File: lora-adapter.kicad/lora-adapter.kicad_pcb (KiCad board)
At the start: 2 copper layers, 36 x 31.9 mm, 6 parts, among them J1 Conn_LoRa, U1 RFM9x_Lora_Breakout

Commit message: LoRa-adapter: Rev 1.00 ready for production
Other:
- board text added: "https://github.com/ bablokb/pcb-pico-datalogger LoRa-Adapter Rev. 1.00"
- board text removed: "https://github.com/ bablokb/pcb-pico-datalogger LoRa-Adapter Rev. 0.90"

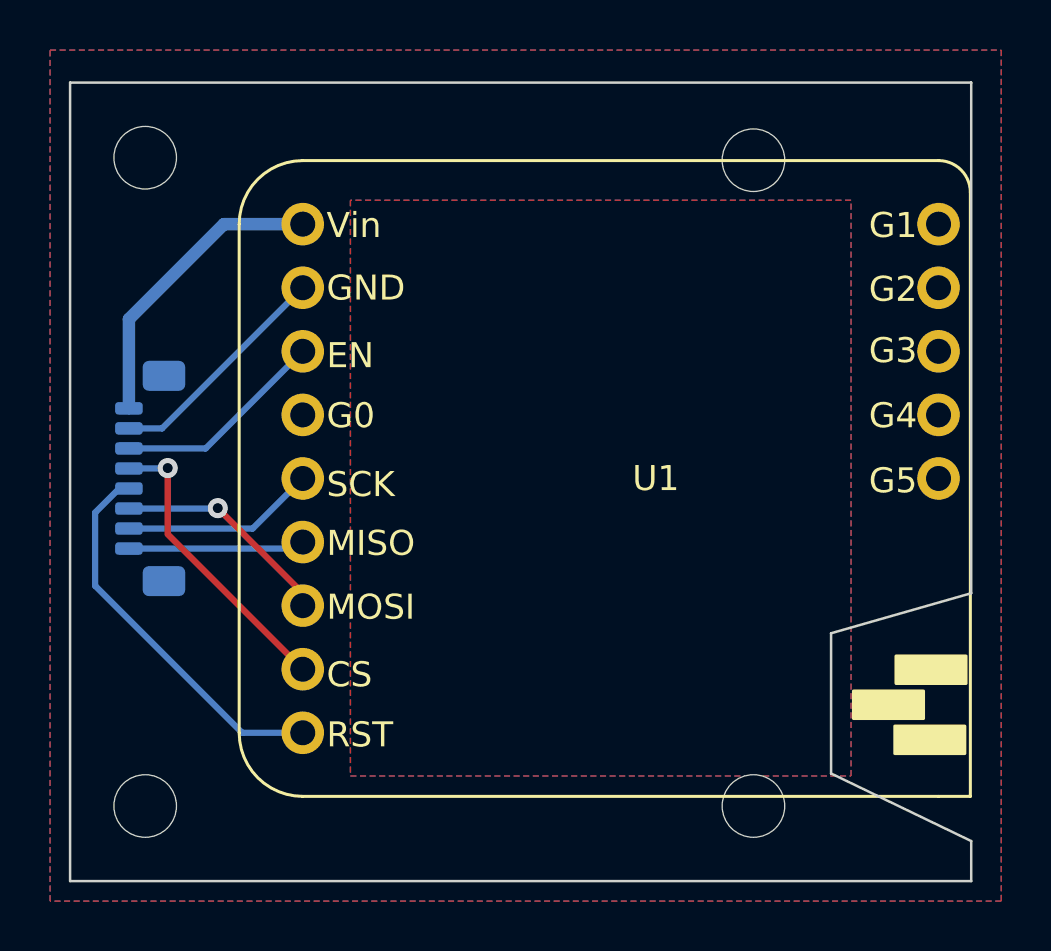
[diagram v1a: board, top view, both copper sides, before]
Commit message: LoRa-Adaper Rev 1.10: add pin-sockets to board (and production files)
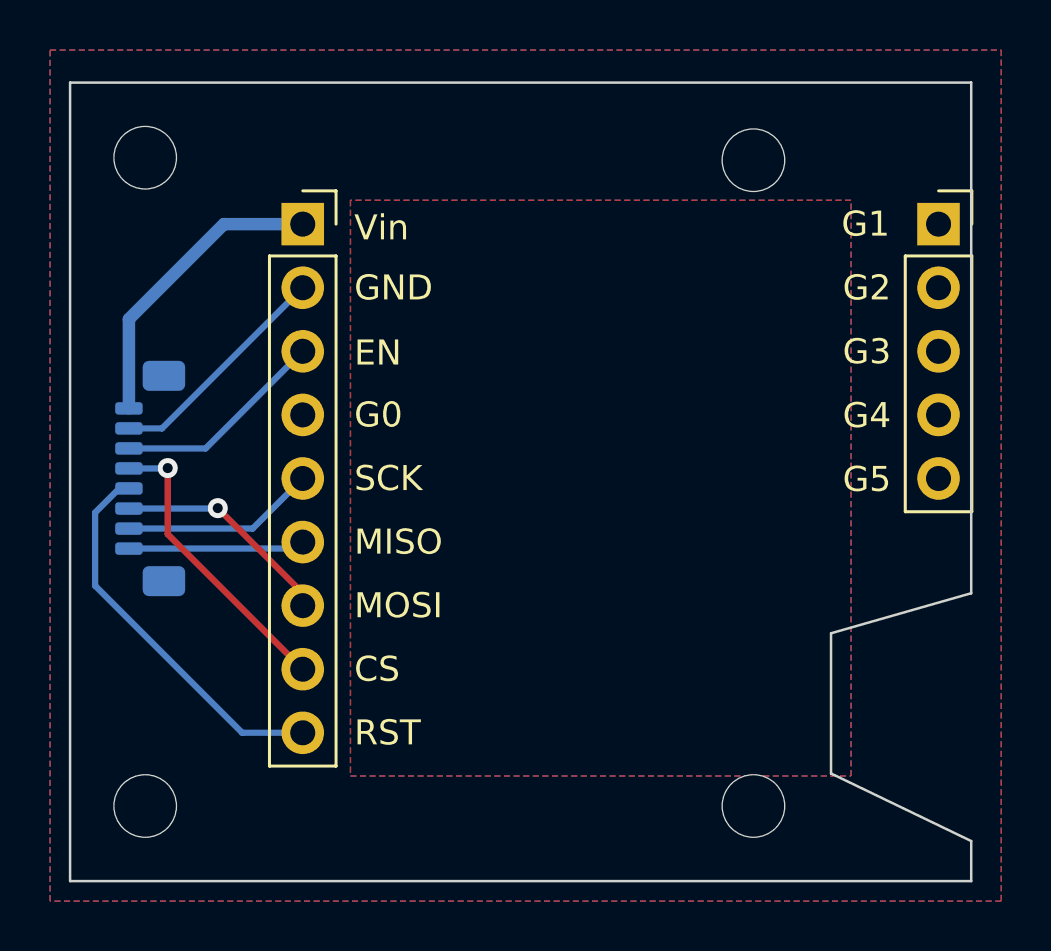
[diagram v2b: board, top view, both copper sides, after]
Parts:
- added J2: Conn_01x05, Connector_PinSocket_2.54mm:PinSocket_1x05_P2.54mm_Vertical, F.Cu at (170.5, 78.0)
- U1: footprint user:RFM9x_Lora_Breakout -> Connector_PinSocket_2.54mm:PinSocket_1x09_P2.54mm_Vertical
- turned U1 to 0 degrees
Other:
- board text added: "3V3"
- board text added: "CS"
- board text added: "EN"
- board text added: "G0"
- board text added: "G1"
- board text added: "G2"
- board text added: "G3"
- board text added: "G4"
- board text added: "G5"
- board text added: "GND"
- board text added: "MISO"
- board text added: "MISO1"
- board text added: "MOSI"
- board text added: "RST"
- board text added: "SCK"
- board text added: "Vin"
- board text added: "https://github.com/ bablokb/pcb-pico-datalogger LoRa-Adapter Rev. 1.10"
- board text removed: "https://github.com/ bablokb/pcb-pico-datalogger LoRa-Adapter Rev. 1.00"

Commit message: LoRa-Adaper Rev 1.20: move SUR-connector to top
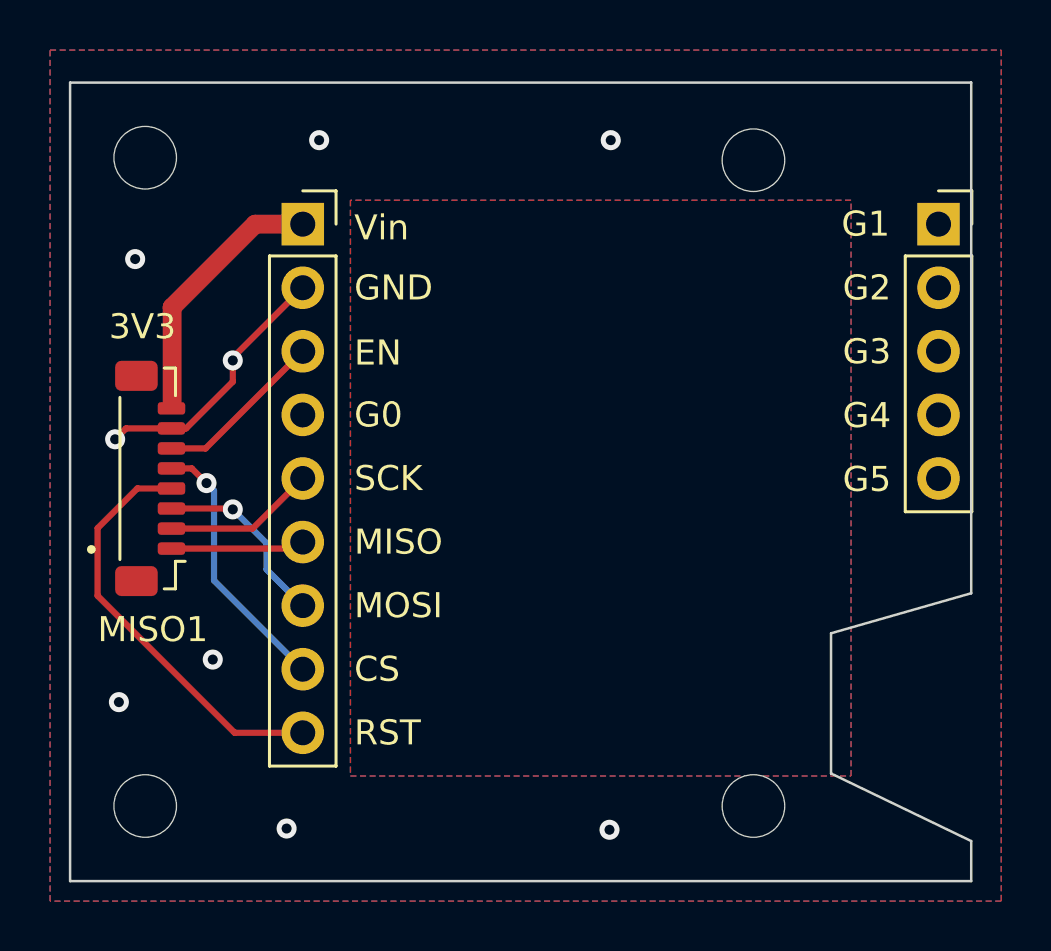
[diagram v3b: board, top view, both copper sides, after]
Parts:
- J1: moved to F.Cu
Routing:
- net /SCLK1: track 7.77 -> 6.07 mm
- net /MISO1: track 7.05 -> 5.35 mm
- net /Lora_EN: track 8.55 -> 6.85 mm
- net +3V3: track 12.1 -> 10.5 mm
- net /MOSI1: track 8.86 -> 7.47 mm
- net /Lora_RST: track 15.4 -> 16.8 mm
- net GND: track 9.27 -> 10.6 mm, vias 0 -> 9
- net /Lora_CS: track 11.8 -> 10.7 mm
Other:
- board text added: "https://github.com/ bablokb/pcb-pico-datalogger LoRa-Adapter Rev. 1.20"
- board text removed: "https://github.com/ bablokb/pcb-pico-datalogger LoRa-Adapter Rev. 1.10"

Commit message: LoRa-Adapter Rev 1.30: turn SURS adapter
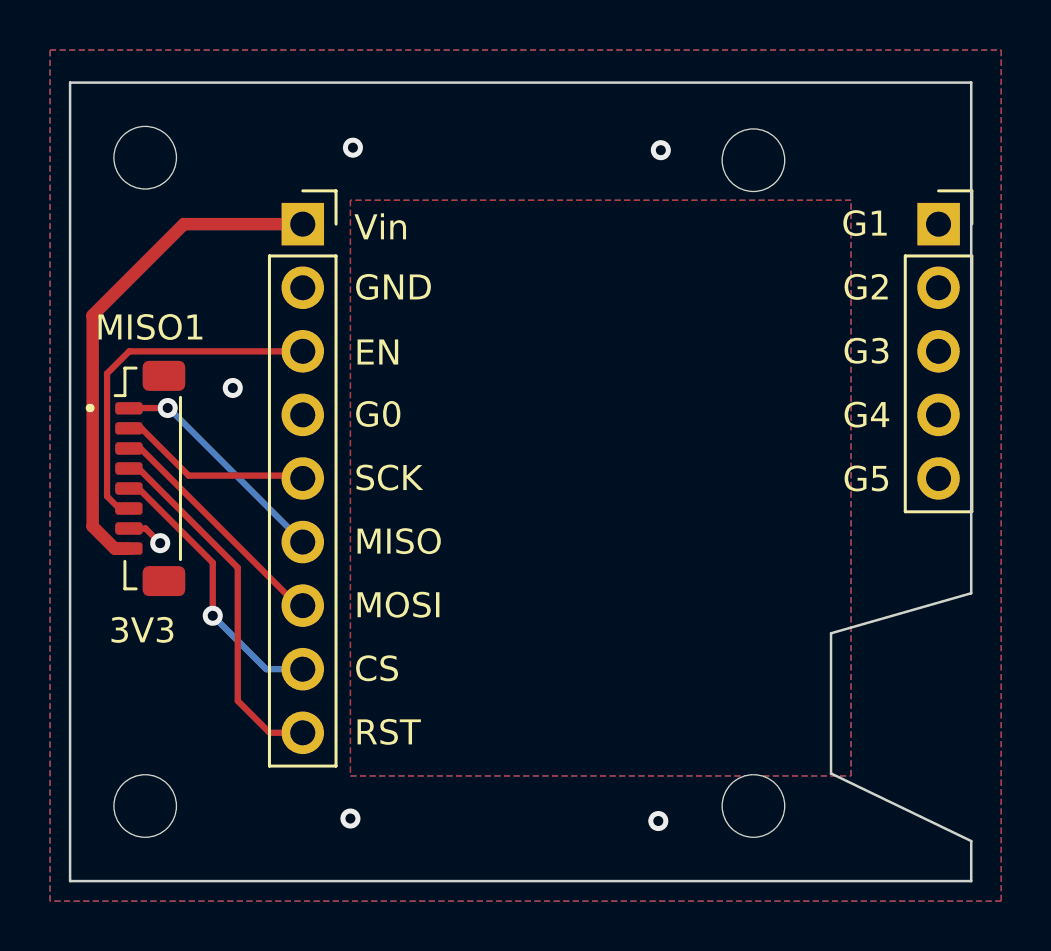
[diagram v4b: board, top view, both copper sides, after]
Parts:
- turned J1 to -90 degrees
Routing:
- net +3V3: track 10.5 -> 20.2 mm
- net GND: track 10.6 -> 1.49 mm, vias 9 -> 6
- net /Lora_EN: track 6.85 -> 14.2 mm
- net /MISO1: track 5.35 -> 9.17 mm, vias 0 -> 1
- net /Lora_RST: track 16.8 -> 14.4 mm
- net /MOSI1: track 7.47 -> 9.55 mm, vias 1 -> 0
- net /SCLK1: track 6.07 -> 7.61 mm
- net /Lora_CS: track 10.7 -> 11.2 mm
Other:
- board text added: "https://github.com/ bablokb/pcb-pico-datalogger LoRa-Adapter Rev. 1.30"
- board text removed: "https://github.com/ bablokb/pcb-pico-datalogger LoRa-Adapter Rev. 1.20"
